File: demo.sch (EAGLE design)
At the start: 4 parts

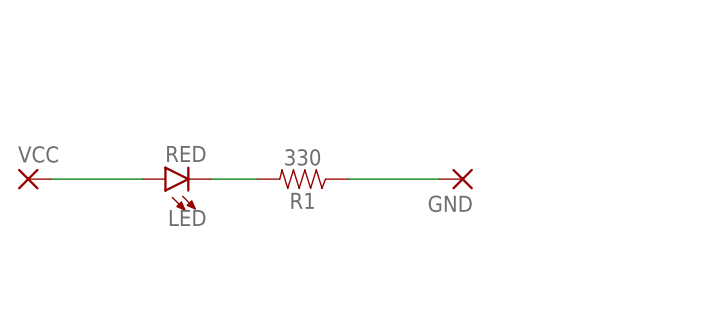
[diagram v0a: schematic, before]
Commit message: Added custom part
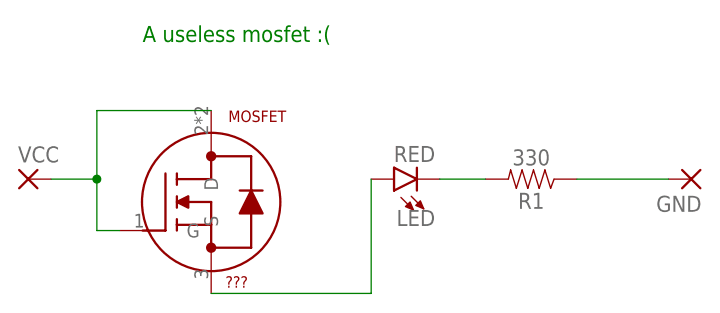
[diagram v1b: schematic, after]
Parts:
- added MOSFET: ???, mylib:CSTM_MOSFET
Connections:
- removed net N$1 (its old number): LED.A, VCC.P
- new net N$3: MOSFET.D, MOSFET.G, VCC.P
- new net N$4: LED.A, MOSFET.S
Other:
- note added: "A useless mosfet :("
- moved on the sheet: GND, LED, R1
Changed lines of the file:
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@@
 <setting verticaltext="up"/>
 </settings>
-<grid distance="0.1" unitdist="inch" unit="inch" style="lines" multiple="1" display="yes" altdistance="0.01" altunitdist="inch" altunit="inch"/>
+<grid distance="0.1" unitdist="inch" unit="inch" style="lines" multiple="1" display="no" altdistance="0.01" altunitdist="inch" altunit="inch"/>
 <layers>
 <layer number="1" name="Top" color="4" fill="1" visible="no" active="no"/>
@@
 <part name="VCC" library="wirepad" library_urn="urn:adsk.eagle:library:412" deviceset="SMD2" device="" package3d_urn="urn:adsk.eagle:package:30839/1"/>
 <part name="GND" library="wirepad" library_urn="urn:adsk.eagle:library:412" deviceset="SMD2" device="" package3d_urn="urn:adsk.eagle:package:30839/1"/>
+<part name="MOSFET" library="mylib" deviceset="CSTM_MOSFET" device="" value="???"/>
 </parts>
 <sheets>
 <sheet>
 <plain>
+<text x="15.24" y="43.18" size="1.778" layer="91">A useless mosfet :(</text>
 </plain>
 <instances>
-<instance part="LED" gate="G$1" x="17.78" y="27.94" smashed="yes" rot="R90">
-<attribute name="NAME" x="22.352" y="24.511" size="1.778" layer="95" font="vector" rot="R180"/>
-<attribute name="VALUE" x="22.352" y="29.845" size="1.778" layer="96" font="vector" rot="R180" align="top-left"/>
-</instance>
-<instance part="R1" gate="G$1" x="33.02" y="27.94" smashed="yes" rot="R180">
-<attribute name="NAME" x="33.02" y="26.416" size="1.778" layer="95" font="vector" rot="R180" align="bottom-center"/>
-<attribute name="VALUE" x="33.02" y="29.464" size="1.778" layer="96" font="vector" rot="R180" align="top-center"/>
+<instance part="LED" gate="G$1" x="43.18" y="27.94" smashed="yes" rot="R90">
+<attribute name="NAME" x="47.752" y="24.511" size="1.778" layer="95" font="vector" rot="R180"/>
+<attribute name="VALUE" x="47.752" y="29.845" size="1.778" layer="96" font="vector" rot="R180" align="top-left"/>
+</instance>
+<instance part="R1" gate="G$1" x="58.42" y="27.94" smashed="yes" rot="R180">
+<attribute name="NAME" x="58.42" y="26.416" size="1.778" layer="95" font="vector" rot="R180" align="bottom-center"/>
+<attribute name="VALUE" x="58.42" y="29.464" size="1.778" layer="96" font="vector" rot="R180" align="top-center"/>
 </instance>
 <instance part="VCC" gate="1" x="2.54" y="27.94" smashed="yes">
@@
 <attribute name="VALUE" x="1.397" y="24.638" size="1.778" layer="96"/>
 </instance>
-<instance part="GND" gate="1" x="50.8" y="27.94" smashed="yes" rot="R180">
-<attribute name="NAME" x="51.943" y="26.0858" size="1.778" layer="95" rot="R180"/>
-<attribute name="VALUE" x="51.943" y="31.242" size="1.778" layer="96" rot="R180"/>
+<instance part="GND" gate="1" x="76.2" y="27.94" smashed="yes" rot="R180">
+<attribute name="NAME" x="77.343" y="26.0858" size="1.778" layer="95" rot="R180"/>
+<attribute name="VALUE" x="77.343" y="31.242" size="1.778" layer="96" rot="R180"/>
+</instance>
+<instance part="MOSFET" gate="G$1" x="22.86" y="25.4" smashed="yes">
+<attribute name="NAME" x="24.765" y="34.29" size="1.27" layer="94"/>
+<attribute name="VALUE" x="24.4475" y="15.875" size="1.27" layer="94"/>
 </instance>
 </instances>
@@
 </busses>
 <nets>
-<net name="N$1" class="0">
-<segment>
-<pinref part="VCC" gate="1" pin="P"/>
-<pinref part="LED" gate="G$1" pin="A"/>
-<wire x1="5.08" y1="27.94" x2="15.24" y2="27.94" width="0.1524" layer="91"/>
-</segment>
-</net>
 <net name="N$2" class="0">
 <segment>
 <pinref part="LED" gate="G$1" pin="C"/>
 <pinref part="R1" gate="G$1" pin="2"/>
-<wire x1="22.86" y1="27.94" x2="27.94" y2="27.94" width="0.1524" layer="91"/>
+<wire x1="48.26" y1="27.94" x2="53.34" y2="27.94" width="0.1524" layer="91"/>
+</segment>
+</net>
+<net name="N$1" class="0">
+<segment>
+<pinref part="GND" gate="1" pin="P"/>
+<pinref part="R1" gate="G$1" pin="1"/>
+<wire x1="63.5" y1="27.94" x2="73.66" y2="27.94" width="0.1524" layer="91"/>
 </segment>
 </net>
 <net name="N$3" class="0">
 <segment>
-<pinref part="R1" gate="G$1" pin="1"/>
-<pinref part="GND" gate="1" pin="P"/>
-<wire x1="38.1" y1="27.94" x2="48.26" y2="27.94" width="0.1524" layer="91"/>
+<pinref part="MOSFET" gate="G$1" pin="D"/>
+<wire x1="22.86" y1="35.56" x2="10.16" y2="35.56" width="0.1524" layer="91"/>
+<wire x1="10.16" y1="35.56" x2="10.16" y2="27.94" width="0.1524" layer="91"/>
+<pinref part="VCC" gate="1" pin="P"/>
+<wire x1="10.16" y1="27.94" x2="5.08" y2="27.94" width="0.1524" layer="91"/>
+<pinref part="MOSFET" gate="G$1" pin="G"/>
+<wire x1="12.7" y1="22.225" x2="10.16" y2="22.225" width="0.1524" layer="91"/>
+<wire x1="10.16" y1="22.225" x2="10.16" y2="27.94" width="0.1524" layer="91"/>
+<junction x="10.16" y="27.94"/>
+</segment>
+</net>
+<net name="N$4" class="0">
+<segment>
+<pinref part="MOSFET" gate="G$1" pin="S"/>
+<pinref part="LED" gate="G$1" pin="A"/>
+<wire x1="22.86" y1="15.24" x2="40.64" y2="15.24" width="0.1524" layer="91"/>
+<wire x1="40.64" y1="15.24" x2="40.64" y2="27.94" width="0.1524" layer="91"/>
 </segment>
 </net>
@@
 </sheet>
 </sheets>
+<errors>
+</errors>
 </schematic>
 </drawing>
